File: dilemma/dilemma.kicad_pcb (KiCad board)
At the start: 2 copper layers, 154.5 x 108.7 mm, 91 parts, among them J1 S3B-PH-SM4-TB(LF)(SN), J2 Serial, J3 BATTERY_CONN_DEANS, J5 S3B-PH-SM4-TB(LF)(SN), SW1 SW_Push, SW10 SW_Push, SW11 SW_Push, SW12 SW_Push, SW13 SW_Push, SW14 SW_Push, SW15 SW_Push, SW16 SW_Push, SW17 locked, SW18 SW_Push, SW19 SW_Push, SW2 SW_Push, SW20 SW_Push, SW21 SW_Push, SW26 SW_SPST, SW3 SW_Push, SW37 SW_SPST, SW4 SW_Push, SW5 SW_Push, SW6 SW_Push, SW7 SW_Push, SW8 SW_Push, SW9 SW_Push, U2 eliteC

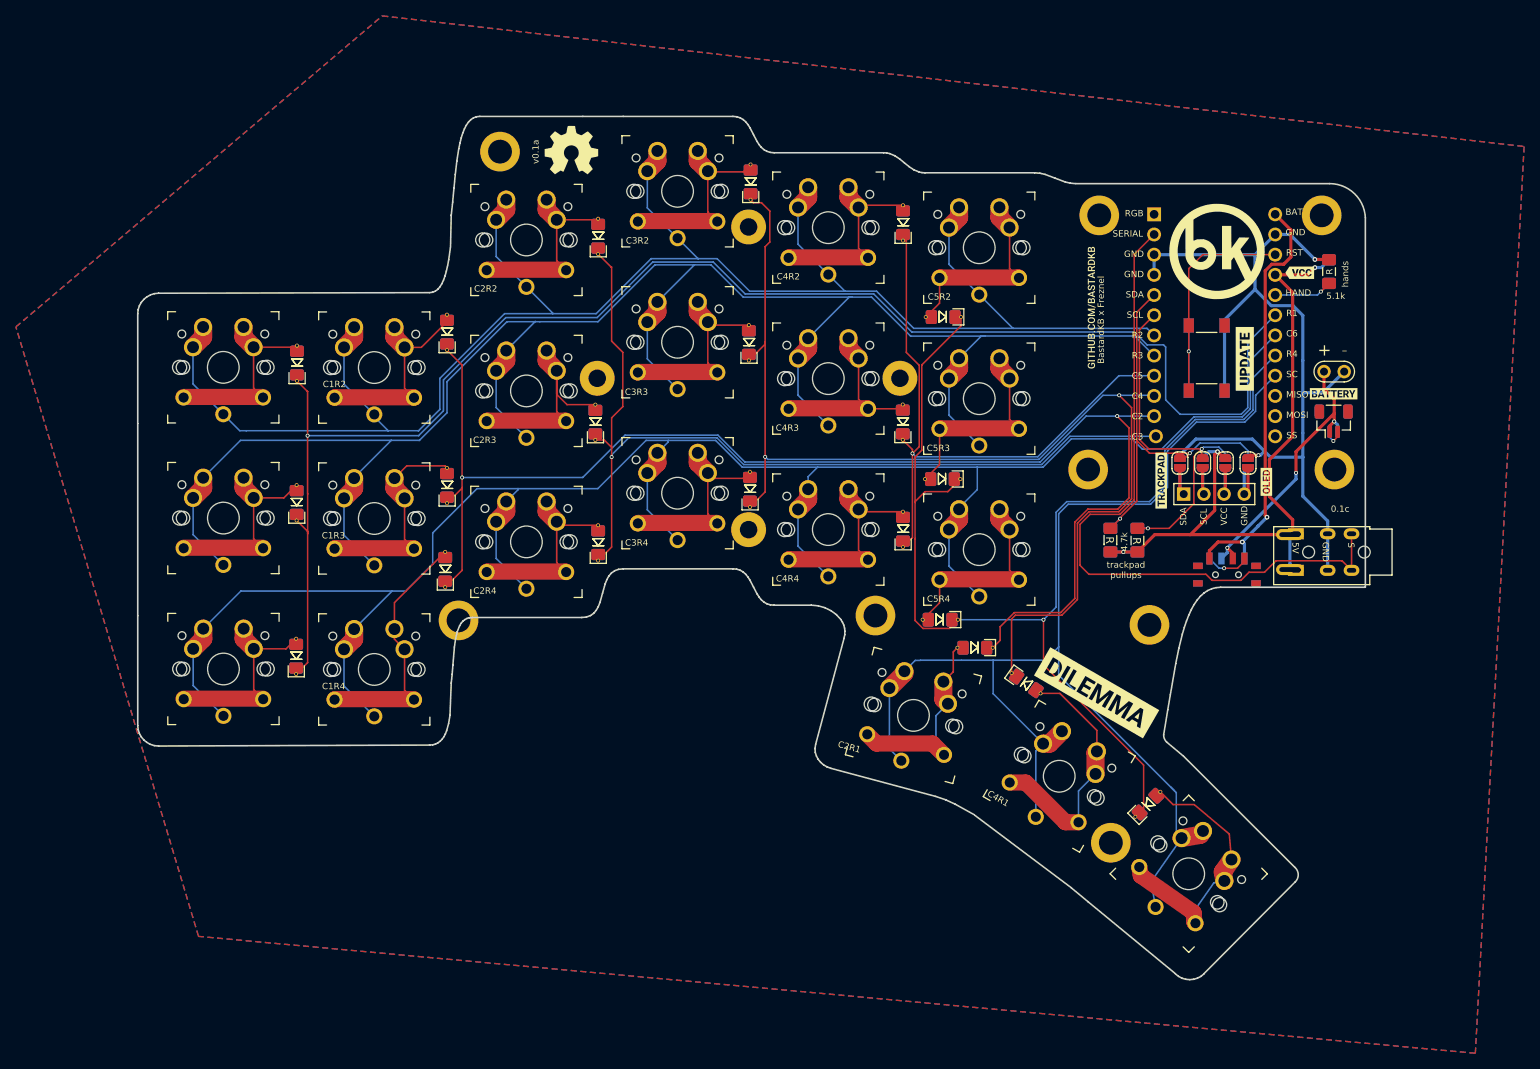
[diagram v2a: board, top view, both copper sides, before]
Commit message: Fix drc errors
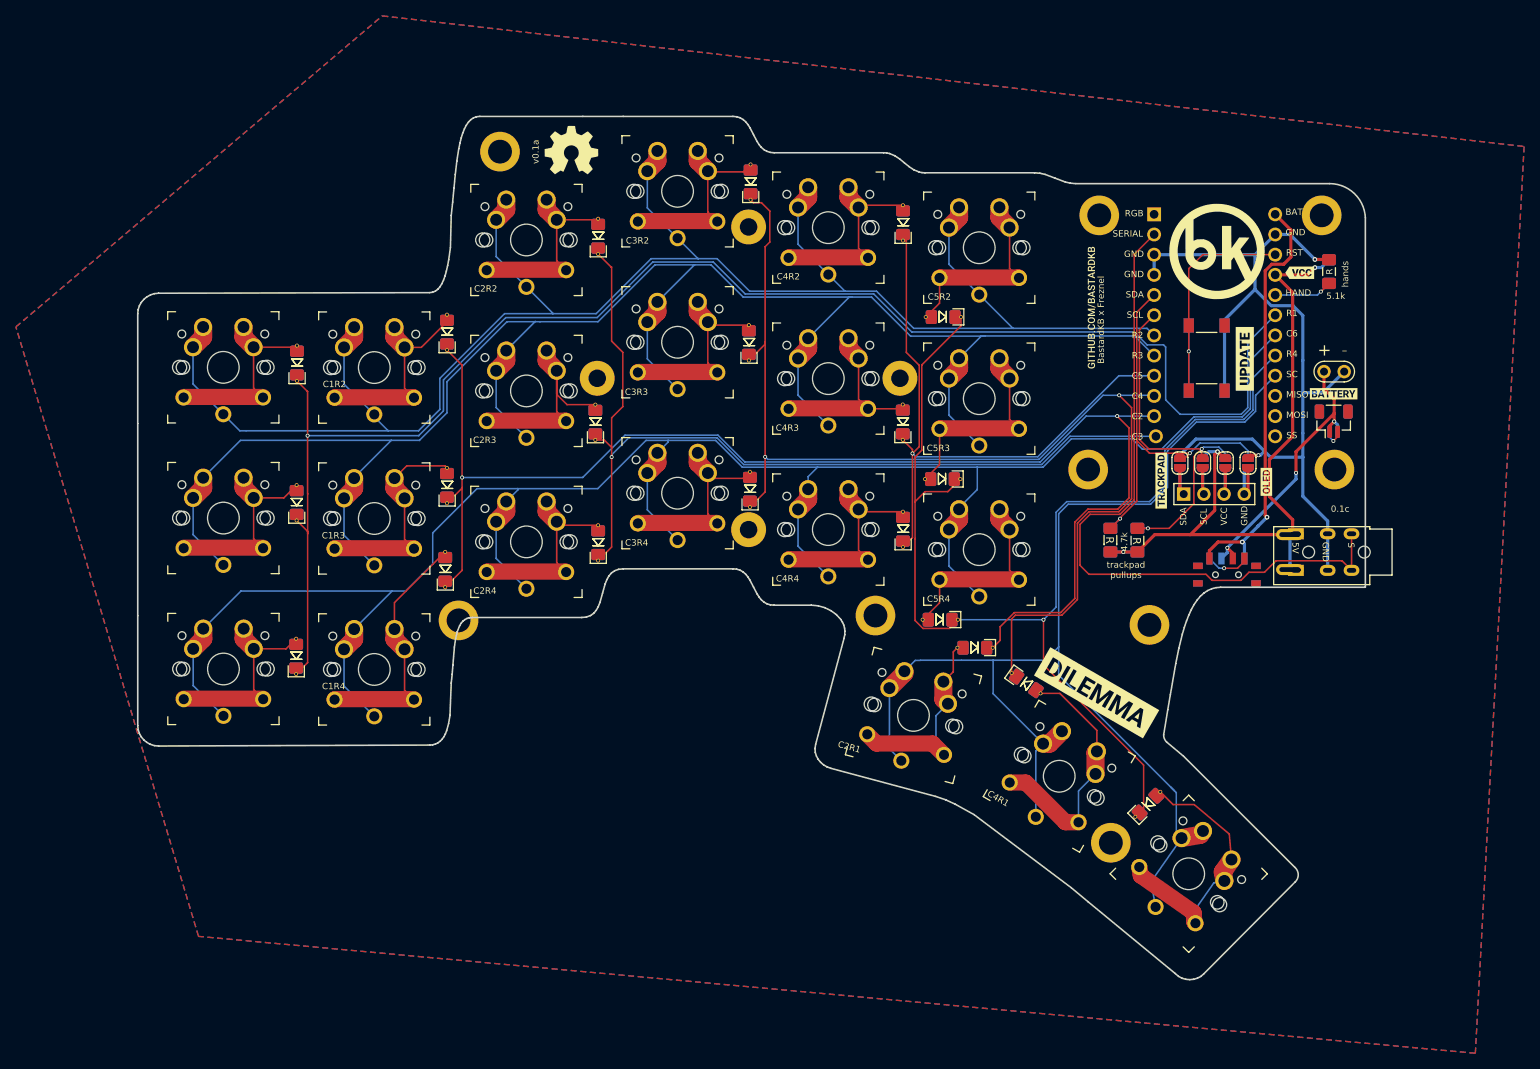
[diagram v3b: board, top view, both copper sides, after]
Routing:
- net row1_l: track 159.4 -> 158.2 mm
- net Net-(D5-Pad2): track 32.9 -> 32.3 mm
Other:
- outline, holes or cut-outs redrawn
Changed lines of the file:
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@@
   (gr_line (start 85.497752 86.503774) (end 85.497752 62.303924) (layer "Edge.Cuts") (width 0.2))
   (gr_line (start 145.527612 80.834704) (end 146.02439 80.655626) (layer "Edge.Cuts") (width 0.2))
-  (gr_line (start 87.104257 102.695049) (end 87.585532 102.84754) (layer "Edge.Cuts") (width 0.2))
+  (gr_line (start 87.057174 102.673513) (end 87.585532 102.84754) (layer "Edge.Cuts") (width 0.2))
   (gr_line (start 124.508809 42.411161) (end 124.640062 41.698026) (layer "Edge.Cuts") (width 0.2))
-  (gr_line (start 216.095756 131.557207) (end 216.510829 131.897641) (layer "Edge.Cuts") (width 0.2))
+  (gr_line (start 216.077975 131.523239) (end 216.510829 131.897641) (layer "Edge.Cuts") (width 0.2))
   (gr_line (start 185.948742 109.243669) (end 187.213057 109.673532) (layer "Edge.Cuts") (width 0.2))
   (gr_line (start 122.242502 45.828957) (end 122.599678 45.783899) (layer "Edge.Cuts") (width 0.2))
@@
   (gr_line (start 183.192709 30.368634) (end 183.857952 30.646179) (layer "Edge.Cuts") (width 0.2))
   (gr_line (start 143.682168 84.815504) (end 144.007483 83.657456) (layer "Edge.Cuts") (width 0.2))
-  (gr_line (start 86.628346 46.373447) (end 87.057174 46.134185) (layer "Edge.Cuts") (width 0.2))
+  (gr_line (start 86.628346 46.373447) (end 87.111373 46.106419) (layer "Edge.Cuts") (width 0.2))
   (gr_line (start 171.998587 85.490414) (end 171.165097 85.252148) (layer "Edge.Cuts") (width 0.2))
   (gr_line (start 216.510829 131.897641) (end 216.958965 132.130124) (layer "Edge.Cuts") (width 0.2))
@@
   (gr_line (start 162.558329 25.067547) (end 163.007318 25.932517) (layer "Edge.Cuts") (width 0.2))
   (gr_line (start 162.025315 24.327025) (end 162.307387 24.674232) (layer "Edge.Cuts") (width 0.2))
-  (gr_line (start 202.99 120.73) (end 205.11722 122.49722) (layer "Edge.Cuts") (width 0.2))
+  (gr_line (start 203 120.73) (end 205.11722 122.49722) (layer "Edge.Cuts") (width 0.2))
   (gr_line (start 145.122248 81.123206) (end 145.527612 80.834704) (layer "Edge.Cuts") (width 0.2))
-  (gr_line (start 122.599678 45.783899) (end 122.926413 45.649367) (layer "Edge.Cuts") (width 0.2))
+  (gr_line (start 122.599678 45.783899) (end 122.969598 45.631704) (layer "Edge.Cuts") (width 0.2))
   (gr_line (start 174.516894 88.453553) (end 174.471825 88.042906) (layer "Edge.Cuts") (width 0.2))
   (gr_line (start 231.21 119.99) (end 219.698129 131.56614) (layer "Edge.Cuts") (width 0.2))
@@
   (gr_line (start 160.41982 23.644993) (end 160.905667 23.690387) (layer "Edge.Cuts") (width 0.2))
   (gr_line (start 144.007483 83.657456) (end 144.332799 82.499408) (layer "Edge.Cuts") (width 0.2))
-  (gr_line (start 122.629452 102.749005) (end 122.98 102.66) (layer "Edge.Cuts") (width 0.2))
+  (gr_line (start 122.629452 102.749005) (end 122.974754 102.646352) (layer "Edge.Cuts") (width 0.2))
   (gr_line (start 163.70725 84.14066) (end 163.989322 84.487866) (layer "Edge.Cuts") (width 0.2))
   (gr_line (start 85.94228 101.748184) (end 86.25444 102.122091) (layer "Edge.Cuts") (width 0.2))
@@
   (gr_line (start 216.993043 88.807278) (end 217.242467 87.959158) (layer "Edge.Cuts") (width 0.2))
   (gr_line (start 125.301582 32.695013) (end 125.469052 30.952768) (layer "Edge.Cuts") (width 0.2))
-  (gr_line (start 190.84 111.6) (end 203 120.73) (layer "Edge.Cuts") (width 0.2))
+  (gr_line (start 190.756769 111.525546) (end 203 120.73) (layer "Edge.Cuts") (width 0.2))
   (gr_line (start 125.078974 93.86013) (end 125.169144 92.707476) (layer "Edge.Cuts") (width 0.2))
   (gr_line (start 163.456308 83.747345) (end 163.70725 84.14066) (layer "Edge.Cuts") (width 0.2))
@@
   (gr_line (start 87.111373 46.106419) (end 87.592648 45.953927) (layer "Edge.Cuts") (width 0.2))
   (gr_line (start 161.702858 24.039633) (end 162.025315 24.327025) (layer "Edge.Cuts") (width 0.2))
-  (gr_line (start 124.96 36.05) (end 124.87 40.11) (layer "Edge.Cuts") (width 0.2))
+  (gr_line (start 124.95825 36.117053) (end 124.859939 40.141974) (layer "Edge.Cuts") (width 0.2))
   (gr_line (start 240.03 36.414983) (end 240.03 82.914983) (layer "Edge.Cuts") (width 0.2))
   (gr_line (start 123.99 44.25) (end 124.180663 43.714244) (layer "Edge.Cuts") (width 0.2))
@@
   (gr_line (start 187.213057 109.673532) (end 188.419957 110.233131) (layer "Edge.Cuts") (width 0.2))
   (gr_line (start 217.43137 132.264164) (end 217.916486 132.307825) (layer "Edge.Cuts") (width 0.2))
-  (gr_line (start 124.349286 43.113002) (end 124.498057 42.452501) (layer "Edge.Cuts") (width 0.2))
+  (gr_line (start 124.349286 43.113002) (end 124.508809 42.411161) (layer "Edge.Cuts") (width 0.2))
   (gr_line (start 182.580013 29.959934) (end 183.192709 30.368634) (layer "Edge.Cuts") (width 0.2))
   (gr_line (start 126.017039 87.753) (end 126.2046 87.44569) (layer "Edge.Cuts") (width 0.2))
@@
   (gr_line (start 214.637208 101.5) (end 215.153575 98.339523) (layer "Edge.Cuts") (width 0.2))
   (gr_line (start 127.252367 86.749871) (end 127.594892 86.720061) (layer "Edge.Cuts") (width 0.2))
-  (gr_line (start 219.322145 131.897654) (end 219.73722 131.55722) (layer "Edge.Cuts") (width 0.2))
+  (gr_line (start 219.322145 131.897654) (end 219.698129 131.56614) (layer "Edge.Cuts") (width 0.2))
   (gr_line (start 162.025315 81.276883) (end 162.307387 81.62409) (layer "Edge.Cuts") (width 0.2))
   (gr_line (start 122.969598 45.631704) (end 123.266526 45.409515) (layer "Edge.Cuts") (width 0.2))
@@
   (segment (start 112.732752 88.178924) (end 117.517752 83.393924) (width 0.2) (layer "B.Cu") (net 5))
   (segment (start 149.482722 64.42752) (end 143.410242 70.5) (width 0.2) (layer "B.Cu") (net 5))
-  (segment (start 118.415252 88.178924) (end 117.812752 88.178924) (width 0.2) (layer "F.Cu") (net 6))
   (segment (start 119.082752 95.868924) (end 120.272752 97.058924) (width 0.2) (layer "F.Cu") (net 6))
   (segment (start 124.2 78.4625) (end 117.812752 84.849748) (width 0.2) (layer "F.Cu") (net 6))
   (segment (start 110.272752 97.058924) (end 110.332263 96.999413) (width 2.032) (layer "F.Cu") (net 6))
   (segment (start 120.213241 96.999413) (end 120.272752 97.058924) (width 2.032) (layer "F.Cu") (net 6))
-  (segment (start 117.812752 89.448924) (end 117.812752 88.178924) (width 0.2) (layer "F.Cu") (net 6))
-  (segment (start 119.082752 90.718924) (end 117.812752 89.448924) (width 0.2) (layer "F.Cu") (net 6))
+  (segment (start 117.812752 89.448924) (end 117.812752 88.178924) (width 2.286) (layer "F.Cu") (net 6))
+  (segment (start 119.082752 90.718924) (end 117.812752 89.448924) (width 2.286) (layer "F.Cu") (net 6))
   (segment (start 117.812752 88.178924) (end 117.812752 84.849748) (width 0.2) (layer "F.Cu") (net 6))
   (segment (start 110.332263 96.999413) (end 120.213241 96.999413) (width 2.032) (layer "F.Cu") (net 6))
@@
   (segment (start 215.115592 65.763592) (end 218.756144 62.12304) (width 0.2) (layer "B.Cu") (net 19))
   (segment (start 201.422 90.424) (end 201.422 93.962) (width 0.2) (layer "B.Cu") (net 19))
-  (segment (start 199.460602 102.600283) (end 199.914326 102.146557) (width 0.2) (layer "B.Cu") (net 19))
   (segment (start 199.746 92.1) (end 201.422 90.424) (width 0.2) (layer "B.Cu") (net 19))
   (segment (start 215.52 108.06) (end 216.223322 108.763322) (width 0.2) (layer "B.Cu") (net 19))
@@
   (segment (start 198.540159 103.520725) (end 199.460602 102.600282) (width 0.2) (layer "B.Cu") (net 19))
   (segment (start 213.056427 119.969392) (end 213.617942 123.153903) (width 0.2) (layer "B.Cu") (net 19))
-  (segment (start 199.460602 102.600283) (end 199.45378 102.601485) (width 0.2) (layer "B.Cu") (net 19))
   (segment (start 202.61848 72.46352) (end 212.987664 72.46352) (width 0.2) (layer "B.Cu") (net 19))
   (segment (start 189.16 92.1) (end 193.17 92.1) (width 0.2) (layer "B.Cu") (net 19))
   (segment (start 216.223322 113.823322) (end 216.891846 114.491846) (width 0.2) (layer "B.Cu") (net 19))
-  (segment (start 201.301903 101.035578) (end 201.830454 101.035578) (width 0.2) (layer "B.Cu") (net 19))
   (segment (start 201.422 73.66) (end 202.61848 72.46352) (width 0.2) (layer "B.Cu") (net 19))
   (segment (start 212.987664 72.46352) (end 215.115592 70.335592) (width 0.2) (layer "B.Cu") (net 19))
